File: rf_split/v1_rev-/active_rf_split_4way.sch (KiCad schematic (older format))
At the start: 34 parts, among them J0 RF_IN, J1 OUT1, J2 OUT2, J3 OUT3, J4 OUT4, U1 BGA2815, U2 LP2985-3.3

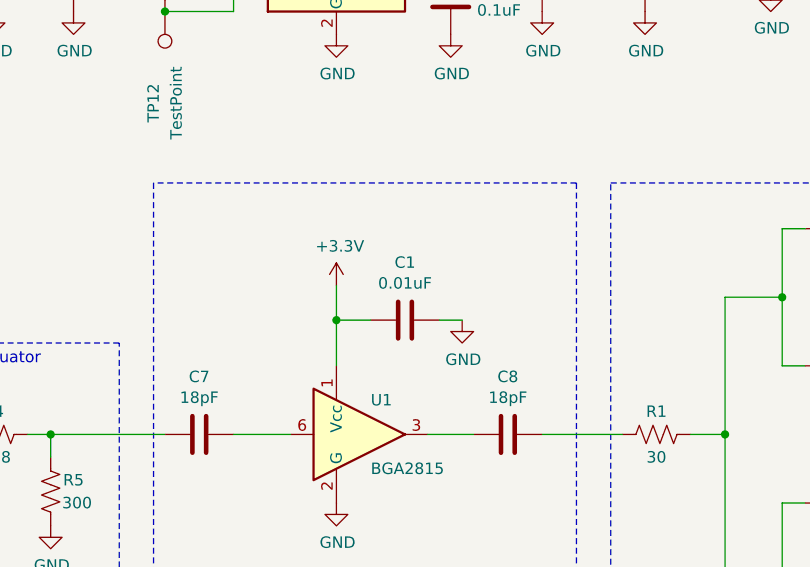
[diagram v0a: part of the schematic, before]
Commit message: updated rf amp decoupling capacitor value
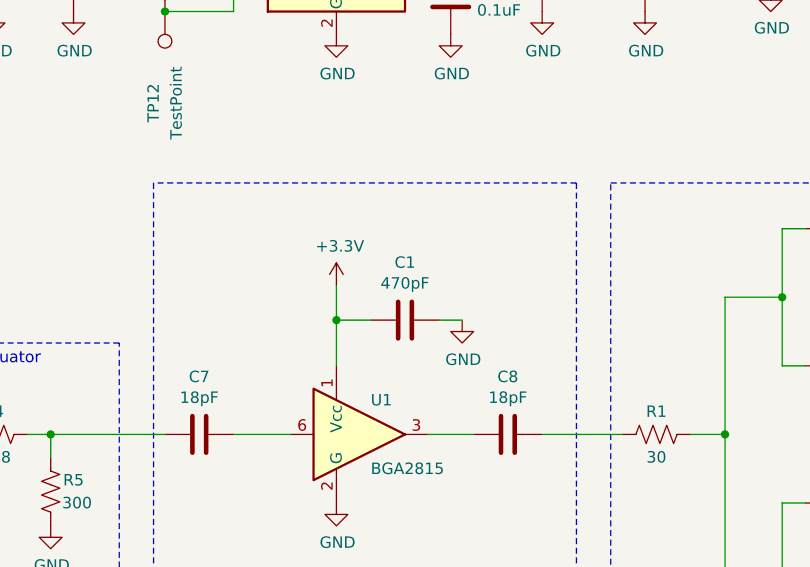
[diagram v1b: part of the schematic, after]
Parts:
- C1: value 0.01uF -> 470pF
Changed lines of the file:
@@
 P 5100 3250
 F 0 "C1" V 4848 3250 50  0000 C CNN
-F 1 "0.01uF" V 4939 3250 50  0000 C CNN
+F 1 "470pF" V 4939 3250 50  0000 C CNN
 F 2 "Capacitor_SMD:C_0805_2012Metric" H 5138 3100 50  0001 C CNN
 F 3 "~" H 5100 3250 50  0001 C CNN
